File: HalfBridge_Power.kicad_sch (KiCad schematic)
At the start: 11 parts, among them Q1 C3M0075120J, Q2 C3M0075120J

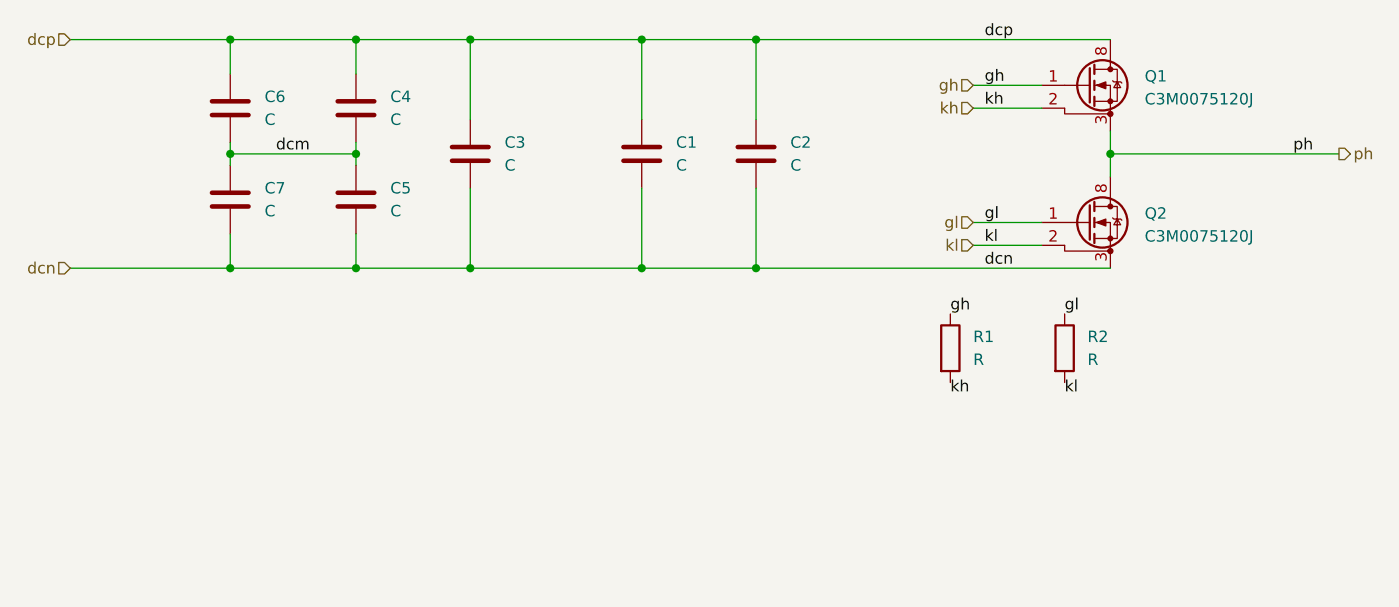
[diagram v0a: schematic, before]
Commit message: gate driver
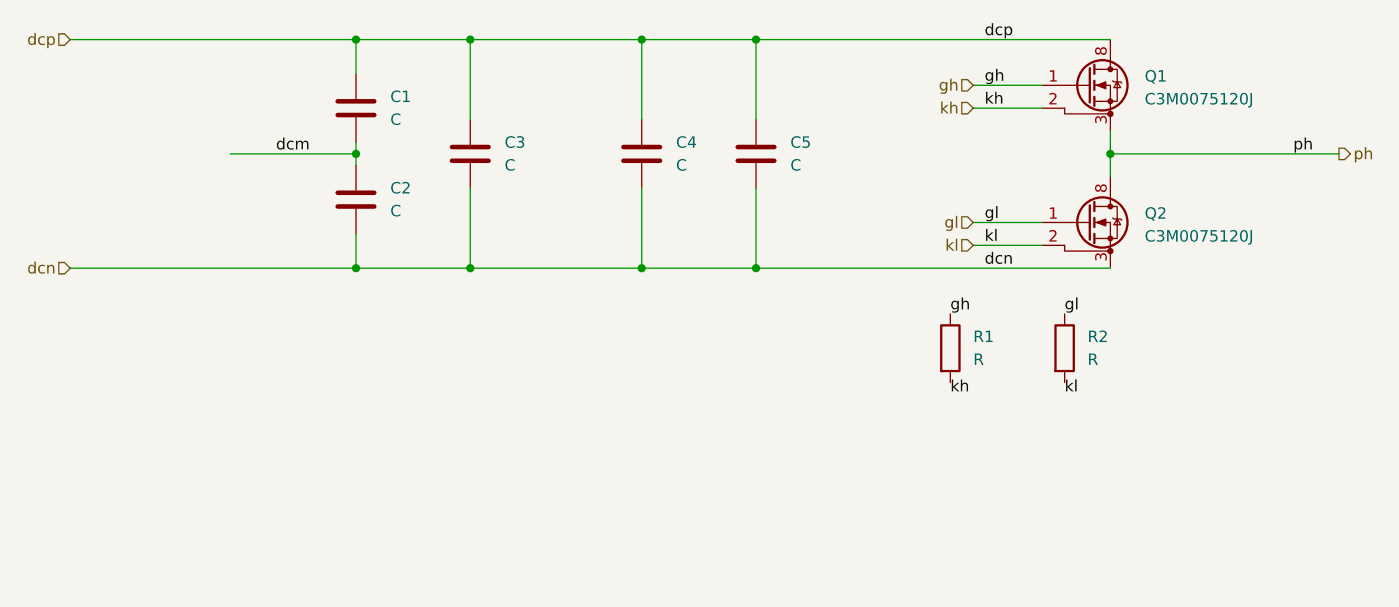
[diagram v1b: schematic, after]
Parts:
- removed C6, C7: C, Capacitor_THT:CP_Radial_D17.0mm_P7.50mm, symbol Device:C
- renumbered C4 to C1, C5 to C2, C1 to C4, C2 to C5
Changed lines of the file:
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@@
-	)
-	(junction
-		(at 132.08 50.8)
-		(diameter 0)
-		(color 0 0 0 0)
 	)
 	(junction
@@
 	)
 	(junction
-		(at 132.08 38.1)
-		(diameter 0)
-		(color 0 0 0 0)
-	)
-	(junction
 		(at 190.5 38.1)
-		(diameter 0)
-		(color 0 0 0 0)
-	)
-	(junction
-		(at 132.08 63.5)
 		(diameter 0)
 		(color 0 0 0 0)
@@
 	(wire
 		(pts
-			(xy 132.08 63.5) (xy 146.05 63.5)
+			(xy 114.3 63.5) (xy 146.05 63.5)
 		)
 		(stroke
@@
 	(wire
 		(pts
-			(xy 132.08 50.8) (xy 132.08 52.07)
-		)
-		(stroke
-			(width 0)
-			(type default)
-		)
-	)
-	(wire
-		(pts
 			(xy 177.8 38.1) (xy 177.8 46.99)
 		)
@@
 	(wire
 		(pts
-			(xy 132.08 49.53) (xy 132.08 50.8)
-		)
-		(stroke
-			(width 0)
-			(type default)
-		)
-	)
-	(wire
-		(pts
 			(xy 190.5 63.5) (xy 229.87 63.5)
 		)
@@
 	(wire
 		(pts
-			(xy 114.3 63.5) (xy 132.08 63.5)
-		)
-		(stroke
-			(width 0)
-			(type default)
-		)
-	)
-	(wire
-		(pts
-			(xy 132.08 38.1) (xy 132.08 41.91)
-		)
-		(stroke
-			(width 0)
-			(type default)
-		)
-	)
-	(wire
-		(pts
 			(xy 214.63 43.18) (xy 222.25 43.18)
 		)
@@
 	(wire
 		(pts
-			(xy 132.08 38.1) (xy 146.05 38.1)
+			(xy 114.3 38.1) (xy 146.05 38.1)
 		)
 		(stroke
@@
 	(wire
 		(pts
-			(xy 114.3 38.1) (xy 132.08 38.1)
-		)
-		(stroke
-			(width 0)
-			(type default)
-		)
-	)
-	(wire
-		(pts
 			(xy 177.8 38.1) (xy 190.5 38.1)
 		)
@@
 		(pts
 			(xy 146.05 59.69) (xy 146.05 63.5)
-		)
-		(stroke
-			(width 0)
-			(type default)
-		)
-	)
-	(wire
-		(pts
-			(xy 132.08 59.69) (xy 132.08 63.5)
 		)
 		(stroke
@@
 			)
 			(justify right)
-		)
-	)
-	(symbol
-		(lib_id "Device:C")
-		(at 132.08 45.72 0)
-		(unit 1)
-		(exclude_from_sim no)
-		(in_bom yes)
-		(on_board yes)
-		(dnp no)
-		(fields_autoplaced yes)
-		(property "Reference" "C6"
-			(at 135.89 44.4499 0)
-			(effects
-				(font
-					(size 1.27 1.27)
-				)
-				(justify left)
-			)
-		)
-		(property "Value" "C"
-			(at 135.89 46.9899 0)
-			(effects
-				(font
-					(size 1.27 1.27)
-				)
-				(justify left)
-			)
-		)
-		(property "Footprint" "Capacitor_THT:CP_Radial_D17.0mm_P7.50mm"
-			(at 133.0452 49.53 0)
-			(effects
-				(font
-					(size 1.27 1.27)
-				)
-				(hide yes)
-			)
-		)
-		(property "Datasheet" "~"
-			(at 132.08 45.72 0)
-			(effects
-				(font
-					(size 1.27 1.27)
-				)
-				(hide yes)
-			)
-		)
-		(property "Description" "Unpolarized capacitor"
-			(at 132.08 45.72 0)
-			(effects
-				(font
-					(size 1.27 1.27)
-				)
-				(hide yes)
-			)
-		)
-		(pin "1"
-		)
-		(pin "2"
-		)
-		(instances
-			(project "HalfBridge_SiC"
-				(path "/3c187ffa-7f66-4861-b077-b6965c821fc2/e430685f-ad0a-4a48-becd-63dd913bcc64"
-					(reference "C6")
-					(unit 1)
-				)
-			)
 		)
 	)
@@
 		(dnp no)
 		(fields_autoplaced yes)
-		(property "Reference" "C1"
+		(property "Reference" "C4"
 			(at 181.61 49.5299 0)
 			(effects
@@
 			(project "HalfBridge_SiC"
 				(path "/3c187ffa-7f66-4861-b077-b6965c821fc2/e430685f-ad0a-4a48-becd-63dd913bcc64"
-					(reference "C1")
+					(reference "C4")
 					(unit 1)
 				)
@@
 		(dnp no)
 		(fields_autoplaced yes)
-		(property "Reference" "C2"
+		(property "Reference" "C5"
 			(at 194.31 49.5299 0)
 			(effects
@@
 			(project "HalfBridge_SiC"
 				(path "/3c187ffa-7f66-4861-b077-b6965c821fc2/e430685f-ad0a-4a48-becd-63dd913bcc64"
-					(reference "C2")
+					(reference "C5")
 					(unit 1)
 				)
@@
 	(symbol
 		(lib_id "Device:C")
-		(at 132.08 55.88 0)
-		(unit 1)
-		(exclude_from_sim no)
-		(in_bom yes)
-		(on_board yes)
-		(dnp no)
-		(fields_autoplaced yes)
-		(property "Reference" "C7"
-			(at 135.89 54.6099 0)
-			(effects
-				(font
-					(size 1.27 1.27)
-				)
-				(justify left)
-			)
-		)
-		(property "Value" "C"
-			(at 135.89 57.1499 0)
-			(effects
-				(font
-					(size 1.27 1.27)
-				)
-				(justify left)
-			)
-		)
-		(property "Footprint" "Capacitor_THT:CP_Radial_D17.0mm_P7.50mm"
-			(at 133.0452 59.69 0)
-			(effects
-				(font
-					(size 1.27 1.27)
-				)
-				(hide yes)
-			)
-		)
-		(property "Datasheet" "~"
-			(at 132.08 55.88 0)
-			(effects
-				(font
-					(size 1.27 1.27)
-				)
-				(hide yes)
-			)
-		)
-		(property "Description" "Unpolarized capacitor"
-			(at 132.08 55.88 0)
-			(effects
-				(font
-					(size 1.27 1.27)
-				)
-				(hide yes)
-			)
-		)
-		(pin "1"
-		)
-		(pin "2"
-		)
-		(instances
-			(project "HalfBridge_SiC"
-				(path "/3c187ffa-7f66-4861-b077-b6965c821fc2/e430685f-ad0a-4a48-becd-63dd913bcc64"
-					(reference "C7")
-					(unit 1)
-				)
-			)
-		)
-	)
-	(symbol
-		(lib_id "Device:C")
 		(at 146.05 55.88 0)
 		(unit 1)
@@
 		(dnp no)
 		(fields_autoplaced yes)
-		(property "Reference" "C5"
+		(property "Reference" "C2"
 			(at 149.86 54.6099 0)
 			(effects
@@
 			(project "HalfBridge_SiC"
 				(path "/3c187ffa-7f66-4861-b077-b6965c821fc2/e430685f-ad0a-4a48-becd-63dd913bcc64"
-					(reference "C5")
+					(reference "C2")
 					(unit 1)
 				)
@@
 		(dnp no)
 		(fields_autoplaced yes)
-		(property "Reference" "C4"
+		(property "Reference" "C1"
 			(at 149.86 44.4499 0)
 			(effects
@@
 			(project "HalfBridge_SiC"
 				(path "/3c187ffa-7f66-4861-b077-b6965c821fc2/e430685f-ad0a-4a48-becd-63dd913bcc64"
-					(reference "C4")
+					(reference "C1")
 					(unit 1)
 				)

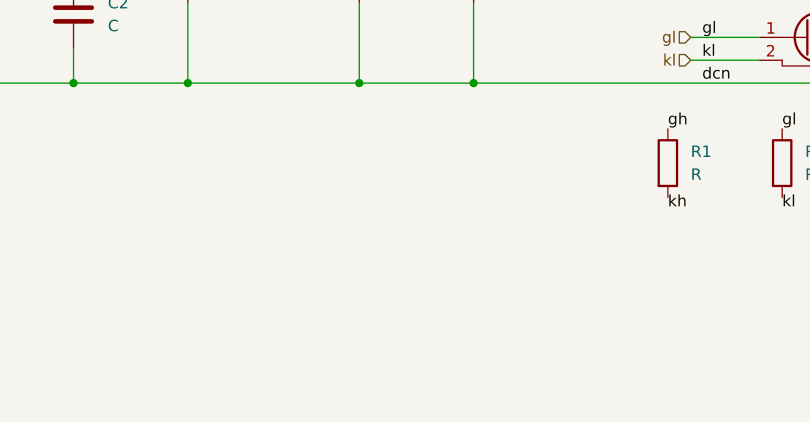
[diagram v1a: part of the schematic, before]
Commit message: symbol library gatedriver
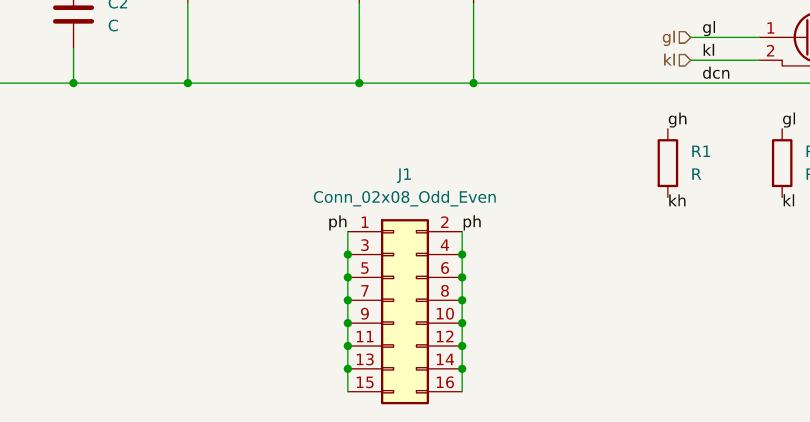
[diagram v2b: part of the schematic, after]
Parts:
- added J1: Conn_02x08_Odd_Even, Connector_PinHeader_2.54mm:PinHeader_2x08_P2.54mm_Vertical_SMD, symbol Connector_Generic:Conn_02x08_Odd_Even
- C1, C2: footprint Capacitor_THT:CP_Radial_D17.0mm_P7.50mm -> Capacitor_THT:CP_Radial_D18.0mm_P7.50mm
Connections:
- net ph: now also J1.1 (Pin_1), J1.10 (Pin_10), J1.11 (Pin_11), J1.12 (Pin_12), J1.13 (Pin_13), J1.14 (Pin_14), J1.15 (Pin_15), J1.16 (Pin_16), J1.2 (Pin_2), J1.3 (Pin_3), J1.4 (Pin_4), J1.5 (Pin_5), J1.6 (Pin_6), J1.7 (Pin_7), J1.8 (Pin_8), J1.9 (Pin_9)

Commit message: dc dc 3d
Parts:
- removed C2: C, Capacitor_THT:CP_Radial_D18.0mm_P7.50mm, symbol Device:C
- removed C3: C, Capacitor_THT:C_Rect_L31.5mm_W15.0mm_P27.50mm_MKS4, symbol Device:C
- C1: footprint Capacitor_THT:CP_Radial_D18.0mm_P7.50mm -> Capacitor_SMD:C_2220_5750Metric_Pad1.97x5.40mm_HandSolder
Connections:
- net dcm: no longer C1.2
- net dcn: now also C1.2
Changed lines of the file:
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@@
-	)
-	(junction
-		(at 158.75 63.5)
-		(diameter 0)
-		(color 0 0 0 0)
 	)
 	(junction
@@
 	)
 	(junction
-		(at 158.75 38.1)
-		(diameter 0)
-		(color 0 0 0 0)
-	)
-	(junction
 		(at 176.53 87.63)
 		(diameter 0)
@@
 	)
 	(junction
+		(at 166.37 38.1)
+		(diameter 0)
+		(color 0 0 0 0)
+	)
+	(junction
 		(at 176.53 82.55)
 		(diameter 0)
 		(color 0 0 0 0)
 	)
+	(junction
+		(at 166.37 63.5)
+		(diameter 0)
+		(color 0 0 0 0)
+	)
 	(wire
 		(pts
@@
 	(wire
 		(pts
-			(xy 158.75 63.5) (xy 177.8 63.5)
+			(xy 146.05 63.5) (xy 166.37 63.5)
 		)
 		(stroke
@@
 	(wire
 		(pts
-			(xy 158.75 54.61) (xy 158.75 63.5)
-		)
-		(stroke
-			(width 0)
-			(type default)
-		)
-	)
-	(wire
-		(pts
 			(xy 177.8 38.1) (xy 177.8 46.99)
 		)
@@
 	(wire
 		(pts
+			(xy 166.37 38.1) (xy 177.8 38.1)
+		)
+		(stroke
+			(width 0)
+			(type default)
+		)
+	)
+	(wire
+		(pts
 			(xy 176.53 80.01) (xy 176.53 82.55)
 		)
@@
 	(wire
 		(pts
+			(xy 166.37 54.61) (xy 166.37 63.5)
+		)
+		(stroke
+			(width 0)
+			(type default)
+		)
+	)
+	(wire
+		(pts
 			(xy 176.53 87.63) (xy 176.53 90.17)
 		)
@@
 	(wire
 		(pts
+			(xy 166.37 63.5) (xy 177.8 63.5)
+		)
+		(stroke
+			(width 0)
+			(type default)
+		)
+	)
+	(wire
+		(pts
 			(xy 214.63 43.18) (xy 222.25 43.18)
 		)
@@
 	(wire
 		(pts
-			(xy 146.05 38.1) (xy 158.75 38.1)
-		)
-		(stroke
-			(width 0)
-			(type default)
-		)
-	)
-	(wire
-		(pts
-			(xy 146.05 63.5) (xy 158.75 63.5)
-		)
-		(stroke
-			(width 0)
-			(type default)
-		)
-	)
-	(wire
-		(pts
 			(xy 176.53 90.17) (xy 176.53 92.71)
 		)
@@
 	(wire
 		(pts
-			(xy 158.75 38.1) (xy 158.75 46.99)
+			(xy 166.37 38.1) (xy 166.37 46.99)
 		)
 		(stroke
@@
 	(wire
 		(pts
-			(xy 158.75 38.1) (xy 177.8 38.1)
+			(xy 146.05 38.1) (xy 166.37 38.1)
 		)
 		(stroke
@@
 	(symbol
 		(lib_id "Device:C")
-		(at 146.05 55.88 0)
+		(at 166.37 50.8 0)
 		(unit 1)
 		(exclude_from_sim no)
@@
 		(dnp no)
 		(fields_autoplaced yes)
-		(property "Reference" "C2"
-			(at 149.86 54.6099 0)
+		(property "Reference" "C1"
+			(at 170.18 49.5299 0)
 			(effects
 				(font
@@
 		)
 		(property "Value" "C"
-			(at 149.86 57.1499 0)
-			(effects
-				(font
-					(size 1.27 1.27)
-				)
-				(justify left)
-			)
-		)
-		(property "Footprint" "Capacitor_THT:CP_Radial_D18.0mm_P7.50mm"
-			(at 147.0152 59.69 0)
+			(at 170.18 52.0699 0)
+			(effects
+				(font
+					(size 1.27 1.27)
+				)
+				(justify left)
+			)
+		)
+		(property "Footprint" "Capacitor_SMD:C_2220_5750Metric_Pad1.97x5.40mm_HandSolder"
+			(at 167.3352 54.61 0)
 			(effects
 				(font
@@
 		)
 		(property "Datasheet" "~"
-			(at 146.05 55.88 0)
+			(at 166.37 50.8 0)
 			(effects
 				(font
@@
 		)
 		(property "Description" "Unpolarized capacitor"
-			(at 146.05 55.88 0)
-			(effects
-				(font
-					(size 1.27 1.27)
-				)
-				(hide yes)
-			)
+			(at 166.37 50.8 0)
+			(effects
+				(font
+					(size 1.27 1.27)
+				)
+				(hide yes)
+			)
+		)
+		(pin "2"
 		)
 		(pin "1"
 		)
-		(pin "2"
-		)
 		(instances
-			(project "HalfBridge_SiC"
-				(path "/3c187ffa-7f66-4861-b077-b6965c821fc2/e430685f-ad0a-4a48-becd-63dd913bcc64"
-					(reference "C2")
-					(unit 1)
-				)
-			)
-		)
-	)
-	(symbol
-		(lib_id "Device:C")
-		(at 158.75 50.8 0)
-		(unit 1)
-		(exclude_from_sim no)
-		(in_bom yes)
-		(on_board yes)
-		(dnp no)
-		(fields_autoplaced yes)
-		(property "Reference" "C3"
-			(at 162.56 49.5299 0)
-			(effects
-				(font
-					(size 1.27 1.27)
-				)
-				(justify left)
-			)
-		)
-		(property "Value" "C"
-			(at 162.56 52.0699 0)
-			(effects
-				(font
-					(size 1.27 1.27)
-				)
-				(justify left)
-			)
-		)
-		(property "Footprint" "Capacitor_THT:C_Rect_L31.5mm_W15.0mm_P27.50mm_MKS4"
-			(at 159.7152 54.61 0)
-			(effects
-				(font
-					(size 1.27 1.27)
-				)
-				(hide yes)
-			)
-		)
-		(property "Datasheet" "~"
-			(at 158.75 50.8 0)
-			(effects
-				(font
-					(size 1.27 1.27)
-				)
-				(hide yes)
-			)
-		)
-		(property "Description" "Unpolarized capacitor"
-			(at 158.75 50.8 0)
-			(effects
-				(font
-					(size 1.27 1.27)
-				)
-				(hide yes)
-			)
-		)
-		(pin "1"
-		)
-		(pin "2"
-		)
-		(instances
-			(project ""
-				(path "/3c187ffa-7f66-4861-b077-b6965c821fc2/e430685f-ad0a-4a48-becd-63dd913bcc64"
-					(reference "C3")
-					(unit 1)
-				)
-			)
-		)
-	)
-	(symbol
-		(lib_id "Device:C")
-		(at 146.05 45.72 0)
-		(unit 1)
-		(exclude_from_sim no)
-		(in_bom yes)
-		(on_board yes)
-		(dnp no)
-		(fields_autoplaced yes)
-		(property "Reference" "C1"
-			(at 149.86 44.4499 0)
-			(effects
-				(font
-					(size 1.27 1.27)
-				)
-				(justify left)
-			)
-		)
-		(property "Value" "C"
-			(at 149.86 46.9899 0)
-			(effects
-				(font
-					(size 1.27 1.27)
-				)
-				(justify left)
-			)
-		)
-		(property "Footprint" "Capacitor_THT:CP_Radial_D18.0mm_P7.50mm"
-			(at 147.0152 49.53 0)
-			(effects
-				(font
-					(size 1.27 1.27)
-				)
-				(hide yes)
-			)
-		)
-		(property "Datasheet" "~"
-			(at 146.05 45.72 0)
-			(effects
-				(font
-					(size 1.27 1.27)
-				)
-				(hide yes)
-			)
-		)
-		(property "Description" "Unpolarized capacitor"
-			(at 146.05 45.72 0)
-			(effects
-				(font
-					(size 1.27 1.27)
-				)
-				(hide yes)
-			)
-		)
-		(pin "1"
-		)
-		(pin "2"
-		)
-		(instances

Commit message: new optical diff xor
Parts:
- renumbered C4 to C2, C5 to C3, J1 to J2, R1 to R2, R2 to R3
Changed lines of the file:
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@@
 		(dnp no)
 		(fields_autoplaced yes)
-		(property "Reference" "C4"
+		(property "Reference" "C2"
 			(at 181.61 49.5299 0)
 			(effects
@@
 			(project "HalfBridge_SiC"
 				(path "/3c187ffa-7f66-4861-b077-b6965c821fc2/e430685f-ad0a-4a48-becd-63dd913bcc64"
-					(reference "C4")
+					(reference "C2")
 					(unit 1)
 				)
@@
 		(dnp no)
 		(fields_autoplaced yes)
-		(property "Reference" "R2"
+		(property "Reference" "R3"
 			(at 227.33 71.1199 0)
 			(effects
@@
 			(project "HalfBridge_SiC"
 				(path "/3c187ffa-7f66-4861-b077-b6965c821fc2/e430685f-ad0a-4a48-becd-63dd913bcc64"
-					(reference "R2")
+					(reference "R3")
 					(unit 1)
 				)
@@
 		(dnp no)
 		(fields_autoplaced yes)
-		(property "Reference" "R1"
+		(property "Reference" "R2"
 			(at 214.63 71.1199 0)
 			(effects
@@
 			(project ""
 				(path "/3c187ffa-7f66-4861-b077-b6965c821fc2/e430685f-ad0a-4a48-becd-63dd913bcc64"
-					(reference "R1")
+					(reference "R2")
 					(unit 1)
 				)
@@
 		(dnp no)
 		(fields_autoplaced yes)
-		(property "Reference" "C5"
+		(property "Reference" "C3"
 			(at 194.31 49.5299 0)
 			(effects
@@
 			(project "HalfBridge_SiC"
 				(path "/3c187ffa-7f66-4861-b077-b6965c821fc2/e430685f-ad0a-4a48-becd-63dd913bcc64"
-					(reference "C5")
+					(reference "C3")
 					(unit 1)
 				)
@@
 		(dnp no)
 		(fields_autoplaced yes)
-		(property "Reference" "J1"
+		(property "Reference" "J2"
 			(at 182.88 73.66 0)
 			(effects
@@
 			(project ""
 				(path "/3c187ffa-7f66-4861-b077-b6965c821fc2/e430685f-ad0a-4a48-becd-63dd913bcc64"
-					(reference "J1")
-					(unit 1)
-				)
+					(reference "J2")
+					(unit 1)
+				)
